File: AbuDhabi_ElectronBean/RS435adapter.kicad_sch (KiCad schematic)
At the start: 3 parts, among them SW1 SW_DPST, SW3 SW_DPST_x2, U4 MAX485ESA_T

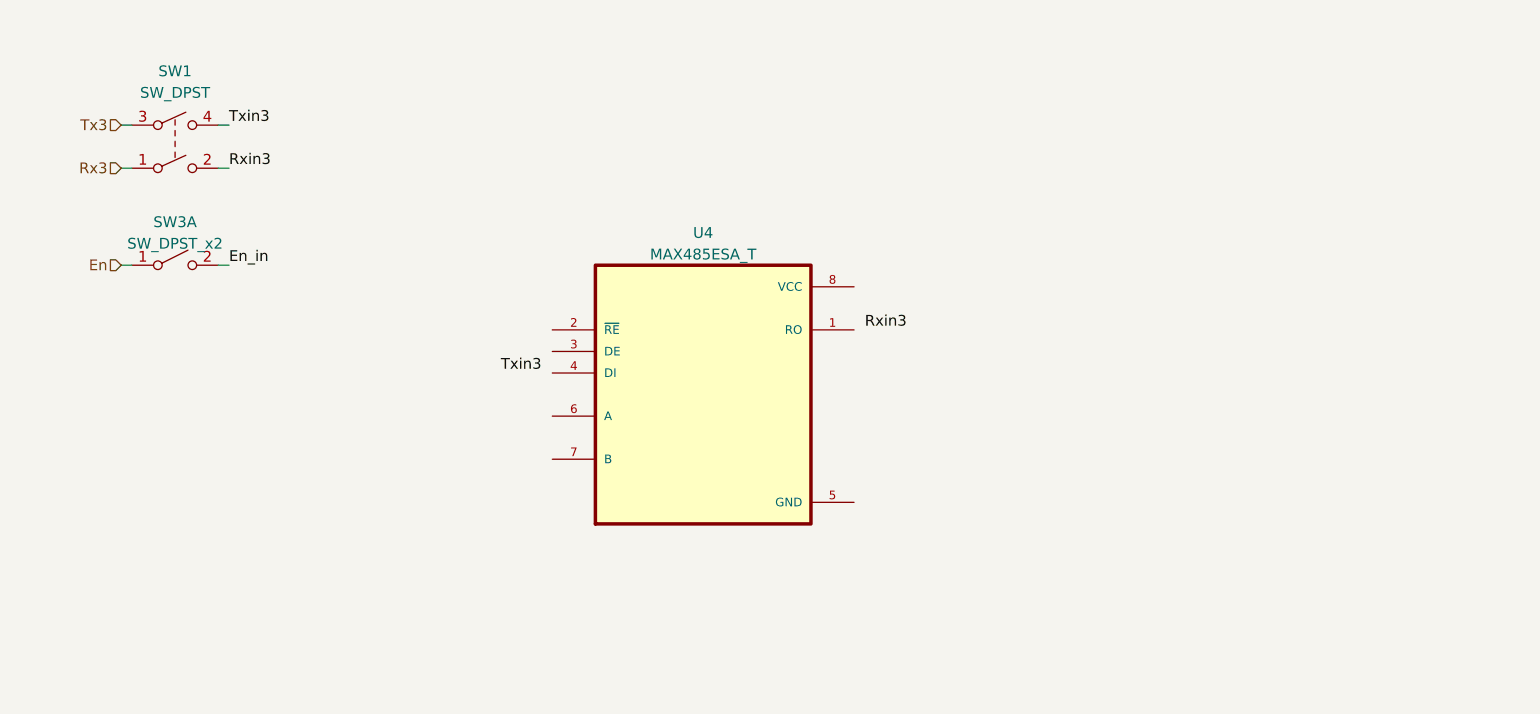
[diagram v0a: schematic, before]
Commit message: RS232 interface changes (completed) and RS485 interface in working...
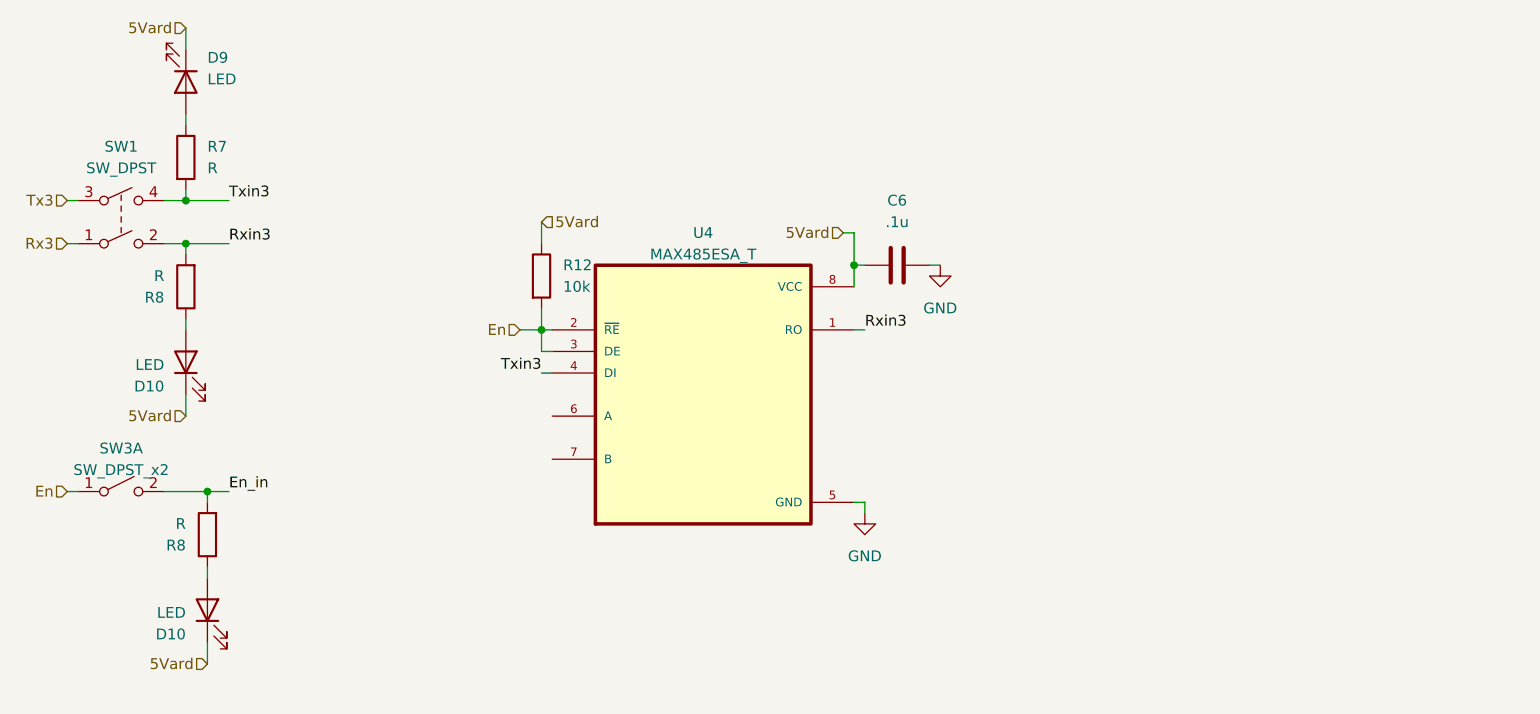
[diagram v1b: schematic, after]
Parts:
- added C6: .1u, symbol Device:C
- added D10 (x2), D9: LED, symbol Device:LED
- added R12: 10k, symbol Device:R
- added R7, R8 (x2): R, symbol Device:R
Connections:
- net En: now also U4.2 (~{RE}), U4.3 (DE), R12.2
- net En_in: now also R8.2
- net Rxin3: now also U4.1 (RO), R8.2
- net Txin3: now also U4.4 (DI), R7.2
- net GND: now reaches U4.5 (GND)
- net GND: now also C6.2
- net 5Vard: now reaches U4.8 (VCC)
- net 5Vard: now also C6.1, D10.1 (K), D10.1 (K), D9.1 (K), R12.1
- new net: D9.2 (A), R7.1
- new net: D10.2 (A), R8.1 (x2)
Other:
- moved on the sheet: SW1, SW3A

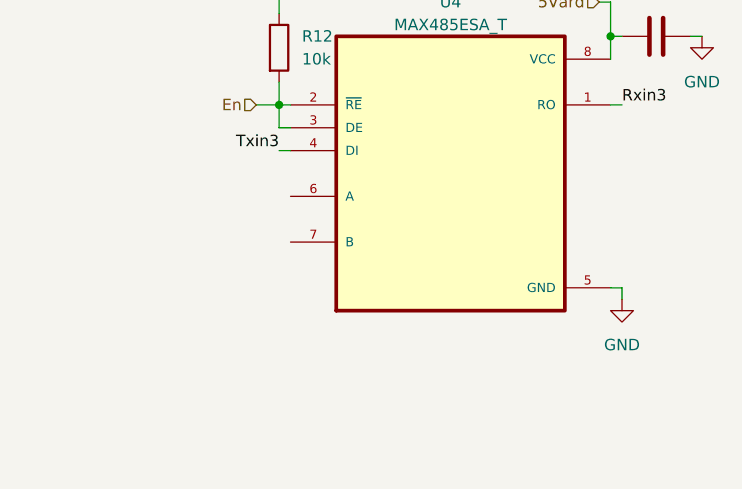
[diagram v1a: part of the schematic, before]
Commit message: Finally understood RS485
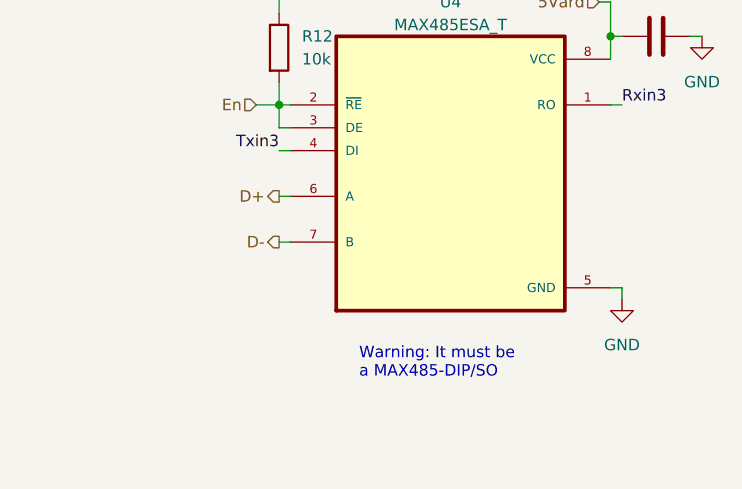
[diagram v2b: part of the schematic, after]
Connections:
- net D+: now reaches U4.6 (A)
- net D-: now reaches U4.7 (B)
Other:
- note added: "Warning: It must be a MAX485-DIP/SO"
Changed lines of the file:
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@@
+    (stroke (width 0) (type default))
+  )
+  (wire (pts (xy 76.2 66.04) (xy 77.47 66.04))
+    (stroke (width 0) (type default))
+  )
+  (wire (pts (xy 76.2 60.96) (xy 77.47 60.96))
     (stroke (width 0) (type default))
   )
@@
     (stroke (width 0) (type default))
   )
+  (text "Warning: It must be\na MAX485-DIP/SO" (at 85.09 81.28 0)
+    (effects (font (size 1.27 1.27)) (justify left bottom))
+  )
   (label "Txin3" (at 76.2 55.88 180) (fields_autoplaced)
     (effects (font (size 1.27 1.27)) (justify right bottom))
@@
     (effects (font (size 1.27 1.27)) (justify right))
   )
+  (hierarchical_label "D+" (shape output) (at 76.2 60.96 180) (fields_autoplaced)
+    (effects (font (size 1.27 1.27)) (justify right))
+  )
+  (hierarchical_label "D-" (shape output) (at 76.2 66.04 180) (fields_autoplaced)
+    (effects (font (size 1.27 1.27)) (justify right))
+  )

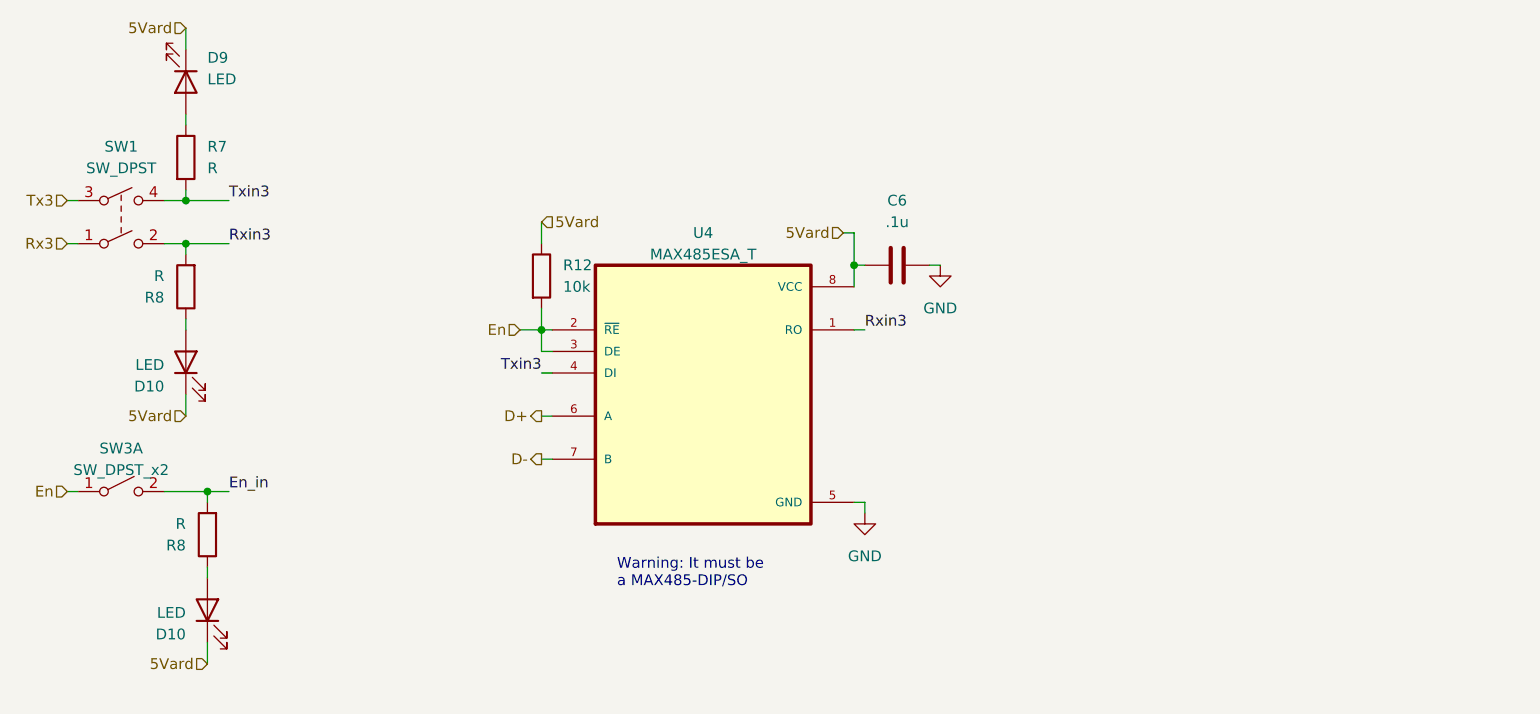
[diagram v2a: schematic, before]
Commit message: Some changes on the full PCB (Robin's folder). Ready to trace.
All changes are being made (from now onwards) in Robins' folder (so it also keeps his changes).
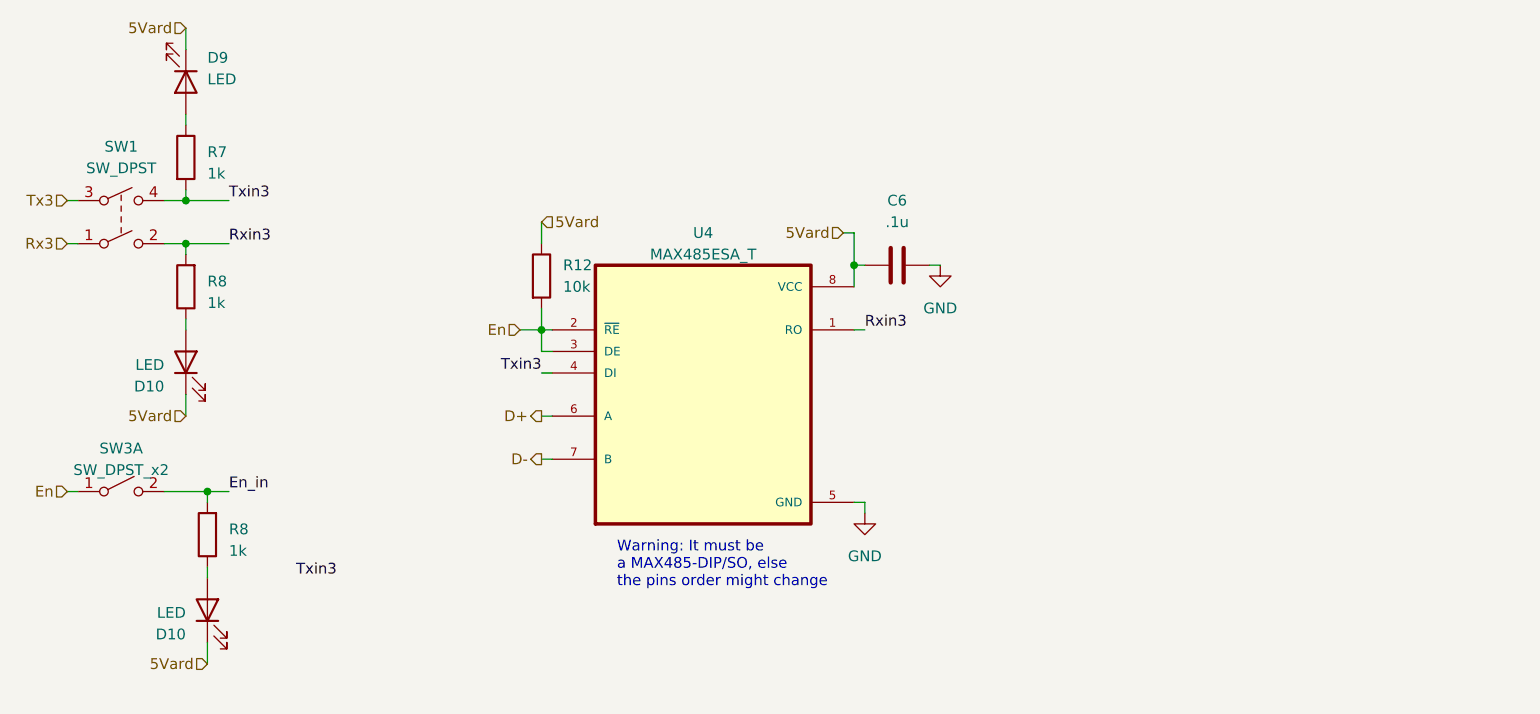
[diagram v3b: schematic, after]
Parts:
- R7, R8: value R -> 1k
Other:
- note added: "Warning: It must be a MAX485-DIP/SO, else the pins order might change"
- note removed: "Warning: It must be a MAX485-DIP/SO"
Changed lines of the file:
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@@
     (stroke (width 0) (type default))
   )
-  (text "Warning: It must be\na MAX485-DIP/SO" (at 85.09 81.28 0)
+  (text "Warning: It must be\na MAX485-DIP/SO, else \nthe pins order might change"
+    (at 85.09 81.28 0)
     (effects (font (size 1.27 1.27)) (justify left bottom))
   )
@@
     (effects (font (size 1.27 1.27)) (justify right bottom))
   )
+  (label "Txin3" (at 52.07 80.01 180) (fields_autoplaced)
+    (effects (font (size 1.27 1.27)) (justify right bottom))
+  )
   (label "Rxin3" (at 114.3 50.8 0) (fields_autoplaced)
     (effects (font (size 1.27 1.27)) (justify left bottom))
@@
   (symbol (lib_id "Device:R") (at 34.29 30.48 0) (unit 1)
     (in_bom yes) (on_board yes) (dnp no) (fields_autoplaced)
-    (property "Reference" "R7" (at 36.83 29.21 0)
-      (effects (font (size 1.27 1.27)) (justify left))
-    )
-    (property "Value" "R" (at 36.83 31.75 0)
+    (property "Reference" "R7" (at 36.83 29.845 0)
+      (effects (font (size 1.27 1.27)) (justify left))
+    )
+    (property "Value" "1k" (at 36.83 32.385 0)
       (effects (font (size 1.27 1.27)) (justify left))
     )
@@
   (symbol (lib_id "Device:R") (at 36.83 74.93 180) (unit 1)
     (in_bom yes) (on_board yes) (dnp no) (fields_autoplaced)
-    (property "Reference" "R8" (at 34.29 76.2 0)
-      (effects (font (size 1.27 1.27)) (justify left))
-    )
-    (property "Value" "R" (at 34.29 73.66 0)
-      (effects (font (size 1.27 1.27)) (justify left))
+    (property "Reference" "R8" (at 39.37 74.295 0)
+      (effects (font (size 1.27 1.27)) (justify right))
+    )
+    (property "Value" "1k" (at 39.37 76.835 0)
+      (effects (font (size 1.27 1.27)) (justify right))
     )
     (property "Footprint" "" (at 38.608 74.93 90)
@@
   (symbol (lib_id "Device:R") (at 34.29 45.72 180) (unit 1)
     (in_bom yes) (on_board yes) (dnp no) (fields_autoplaced)
-    (property "Reference" "R8" (at 31.75 46.99 0)
-      (effects (font (size 1.27 1.27)) (justify left))
-    )
-    (property "Value" "R" (at 31.75 44.45 0)
-      (effects (font (size 1.27 1.27)) (justify left))
+    (property "Reference" "R8" (at 36.83 45.085 0)
+      (effects (font (size 1.27 1.27)) (justify right))
+    )
+    (property "Value" "1k" (at 36.83 47.625 0)
+      (effects (font (size 1.27 1.27)) (justify right))
     )
     (property "Footprint" "" (at 36.068 45.72 90)

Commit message: Main board file updated. Added Arduino code for the LCD
The LCD is not working yet though.
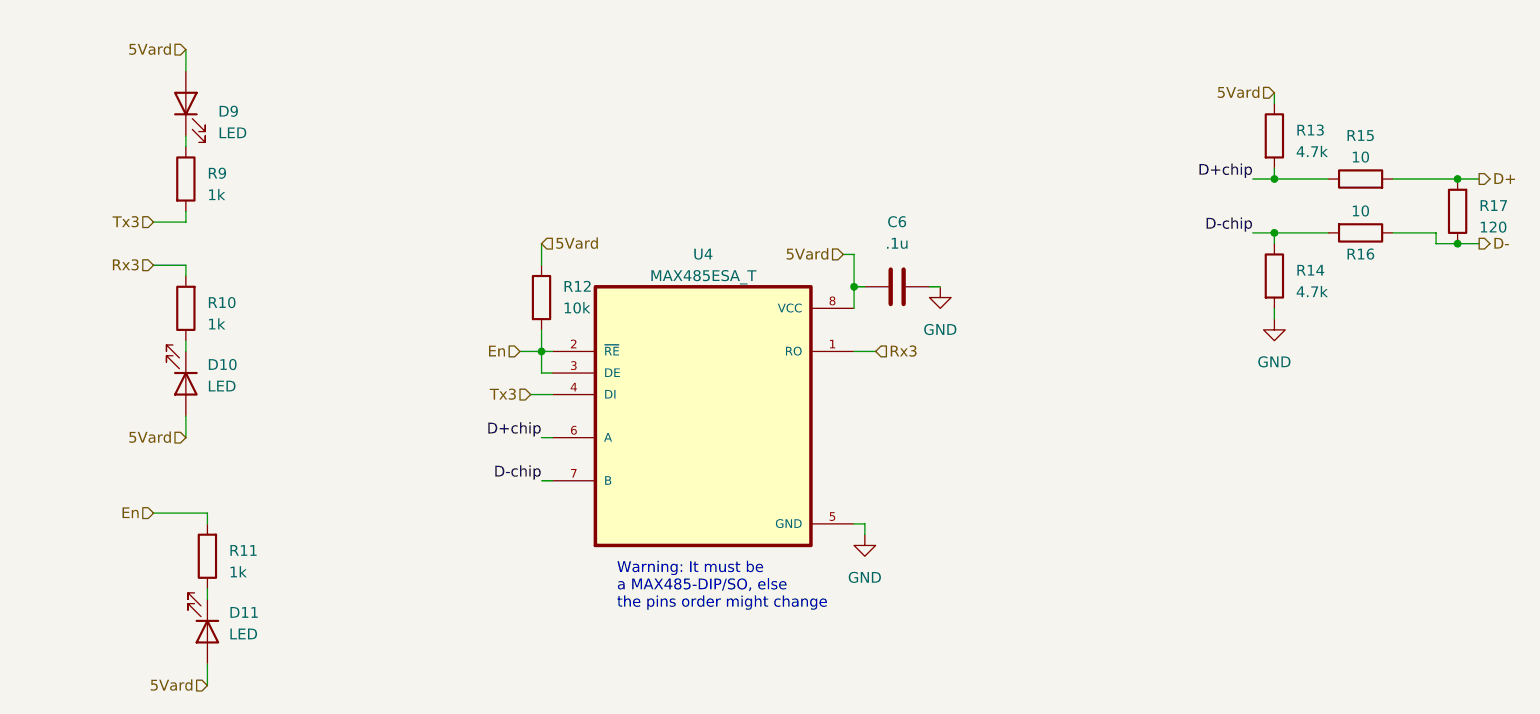
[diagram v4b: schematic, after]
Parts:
- removed D10 (x2): LED, symbol Device:LED
- removed R7, R8 (x2): 1k, symbol Device:R
- removed SW1: SW_DPST, symbol Switch:SW_DPST
- removed SW3: SW_DPST_x2, symbol Switch:SW_DPST_x2
- added D10, D11: LED, LED_SMD:LED_0603_1608Metric, symbol Device:LED
- added R10, R11, R9: 1k, Resistor_SMD:R_0603_1608Metric, symbol Device:R
- added R13, R14: 4.7k, Resistor_SMD:R_0603_1608Metric, symbol Device:R
- added R15, R16: 10, Resistor_SMD:R_0603_1608Metric, symbol Device:R
- added R17: 120, Resistor_SMD:R_0603_1608Metric, symbol Device:R
- C6: footprint (none) -> Capacitor_SMD:C_0603_1608Metric
- D9: footprint (none) -> LED_SMD:LED_0603_1608Metric
- R12: footprint (none) -> Resistor_SMD:R_0603_1608Metric
- U4: footprint MAX485ESA_T:SOIC127P600X175-8N -> MAX485:SOIC127P600X175-8N
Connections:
- net Rxin3 is gone; now on net Rx3: U4.1 (RO)
- net Txin3 is gone; now on net Tx3: U4.4 (DI)
- net 5Vard: now also D9.2 (A), D10.2 (A), D11.2 (A), R13.1; no longer D9.1 (K)
- net D+: now also R15.2, R17.2; no longer U4.6 (A)
- net D-: now also R16.1, R17.1; no longer U4.7 (B)
- net En: now also R11.2
- net GND: now also R14.2
- net Rx3: now also R10.2
- net Tx3: now also R9.2
- new net: D11.1 (K), R11.1
- new net: D9.1 (K), R9.1
- new net: D10.1 (K), R10.1
- new net D+chip: R13.2, R15.1, U4.6 (A)
- new net D-chip: R14.1, R16.2, U4.7 (B)
